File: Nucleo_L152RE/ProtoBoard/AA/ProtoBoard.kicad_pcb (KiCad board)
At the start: 2 copper layers, 7 parts, among them P1 SWD Header, P2 Power, U1 Nucleo-L152RE-CN7, U2 Nucleo-L152RE-CN10, U3 RFM69HW

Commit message: Have all footprints selected for components, now starting to organize parts on board.
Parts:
- added C10: 0.1u, Capacitors_SMD:C_0603, F.Cu at (-41.1, 7.87)
- added C11: 0.1u, Capacitors_SMD:C_0603, F.Cu at (-53.1, 9.65)
- added C12: 0.1u, Capacitors_SMD:C_0603, F.Cu at (-54.4, 16.3)
- added C3: 10uF, Capacitors_SMD:C_0603_HandSoldering, F.Cu at (-37.1, 16.3)
- added C4: 10uF, Capacitors_SMD:C_0603_HandSoldering, F.Cu at (-36.6, 14.0)
- added C5: 22uF, Capacitors_SMD:C_0603_HandSoldering, F.Cu at (-38.1, 6.35)
- added C6: 22uF, Capacitors_SMD:C_0603_HandSoldering, F.Cu at (-41.4, 4.06)
- added C7: 220uF, nucleo:Cap_alum_electro_3.3x3.3, F.Cu at (-42.7, 13.0)
- added C8: 0.1u, Capacitors_SMD:C_0603, F.Cu at (-36.3, 10.7)
- added C9: 0.1p, Capacitors_SMD:C_0603, F.Cu at (-47.2, 8.38)
- added D1: Red, nucleo:LED_0603, F.Cu at (-39.6, 19.8)
- added D2: Green, nucleo:LED_0603, F.Cu at (-42.7, 13.0)
- added J1: EXT1, nucleo:RJ45_SMD, F.Cu at (47.5, 2.54)
- added J2: USB, Connect:USB_B, F.Cu at (22.6, -4.32)
- added J3: EXT2, nucleo:RJ45_SMD, F.Cu at (46.0, -24.1)
- added JP1: Jumper_NC_Small, nucleo:SB_NC, F.Cu at (-48.0, 12.4)
- added JP10, JP11, JP13, JP15, JP16, JP17, JP18, JP19, JP20, JP21, JP22, JP23, JP24, JP25, JP26, JP27, JP28, JP29, JP30, JP31, JP38, JP39, JP4, JP40, JP41, JP42, JP5, JP6, JP7, JP8, JP9: Jumper_NC_Small, nucleo:SB_NC, F.Cu at (-42.7, 13.0)
- added JP12, JP14, JP32, JP33, JP34, JP35, JP36, JP37: Jumper_NO_Small, nucleo:SB_NO, F.Cu at (-42.7, 13.0)
- added JP2: Jumper_NC_Small, nucleo:SB_NC, F.Cu at (-42.2, 18.3)
- added JP3: Jumper_NC_Small, nucleo:SB_NC, F.Cu at (-55.1, 13.2)
- added L1: 4.7uH, nucleo:Inductor_4.7u, F.Cu at (-31.8, 3.56)
- added L2: 10uH, nucleo:Inductor_10u, F.Cu at (-23.9, -3.56)
- added L3, L4: 600 Ohm, Resistors_SMD:R_0603_HandSoldering, F.Cu at (-42.7, 13.0)
- added P10: CONN_01X06, Pin_Headers:Pin_Header_Straight_1x06, F.Cu at (0.00, 21.3)
- added P11: I2C1_B, Pin_Headers:Pin_Header_Straight_1x04, F.Cu at (31.8, 16.3)
- added P12: I2C2_B, Pin_Headers:Pin_Header_Straight_1x04, F.Cu at (36.8, 14.7)
- added P13: SW_1_6, Pin_Headers:Pin_Header_Straight_2x06, F.Cu at (-17.8, 18.3)
- added P14: WS_1_2, Pin_Headers:Pin_Header_Straight_2x02, F.Cu at (-29.2, 15.2)
- added P15: WS_3_4, Pin_Headers:Pin_Header_Straight_2x02, F.Cu at (-29.0, 22.4)
- added P16: MS2, Pin_Headers:Pin_Header_Straight_1x03, F.Cu at (-19.6, 6.60)
- added P17: OW1_B, Pin_Headers:Pin_Header_Straight_1x03, F.Cu at (14.5, 2.03)
- added P18: OW2_B, Pin_Headers:Pin_Header_Straight_1x03, F.Cu at (12.4, -7.62)
- added P19: I2C1_C, Pin_Headers:Pin_Header_Straight_1x04, F.Cu at (41.7, 14.7)
- added P20: I2C2_C, Pin_Headers:Pin_Header_Straight_1x04, F.Cu at (15.0, 18.3)
- added P21: MS3, Pin_Headers:Pin_Header_Straight_1x03, F.Cu at (-11.7, 5.59)
- added P22: OW3_A, Pin_Headers:Pin_Header_Straight_1x03, F.Cu at (8.64, 1.78)
- added P23: OW4_A, Pin_Headers:Pin_Header_Straight_1x03, F.Cu at (17.3, -17.0)
- added P24: MS4, Pin_Headers:Pin_Header_Straight_1x03, F.Cu at (-6.86, 4.83)
- added P25: OW3_B, Pin_Headers:Pin_Header_Straight_1x03, F.Cu at (1.78, -16.0)
- added P26: OW4_B, Pin_Headers:Pin_Header_Straight_1x03, F.Cu at (-3.56, -15.7)
- added P27: RGB1, Pin_Headers:Pin_Header_Straight_1x04, F.Cu at (8.64, 15.7)
- added P28: Ant, Pin_Headers:Pin_Header_Straight_1x01, F.Cu at (18.5, -34.0)
- added P3: SWD Header, Pin_Headers:Pin_Header_Straight_1x06, F.Cu at (-6.86, 18.8)
- added P4: USART1, Pin_Headers:Pin_Header_Straight_1x04, F.Cu at (5.08, 24.6)
- added P5: MS1, Pin_Headers:Pin_Header_Straight_1x03, F.Cu at (-16.3, 6.10)
- added P6: I2C1_A, Pin_Headers:Pin_Header_Straight_1x04, F.Cu at (20.3, 17.8)
- added P7: I2C2_A, Pin_Headers:Pin_Header_Straight_1x04, F.Cu at (25.9, 17.3)
- added P8: OW1_A, Pin_Headers:Pin_Header_Straight_1x03, F.Cu at (6.86, -15.2)
- added P9: OW2_A, Pin_Headers:Pin_Header_Straight_1x03, F.Cu at (12.2, -15.7)
- added Q1: SI2323DS, SMD_Packages:SOT-323, F.Cu at (-42.7, 13.0)
- added R1: 4.7k, Resistors_SMD:R_0603_HandSoldering, F.Cu at (-46.7, 17.5)
- added R10, R9: 33, Resistors_SMD:R_0603_HandSoldering, F.Cu at (-42.7, 13.0)
- added R11, R12, R32, R33, R34, R35, R47, R7: 0, Resistors_SMD:R_0603_HandSoldering, F.Cu at (-42.7, 13.0)
- added R13, R15: 100k, Resistors_SMD:R_0603_HandSoldering, F.Cu at (-42.7, 13.0)
- added R14, R16, R26, R27, R28, R29, R30, R31, R36: 10k, Resistors_SMD:R_0603_HandSoldering, F.Cu at (-42.7, 13.0)
- added R17: 4.7K, Resistors_SMD:R_0603_HandSoldering, F.Cu at (-42.7, 13.0)
- added R18: 2.2K, Resistors_SMD:R_0603_HandSoldering, F.Cu at (-42.7, 13.0)
- added R19: 680, Resistors_SMD:R_0603_HandSoldering, F.Cu at (-42.7, 13.0)
- added R2: 4.7k, Resistors_SMD:R_0603_HandSoldering, F.Cu at (-52.1, 6.10)
- added R20: 390, Resistors_SMD:R_0603_HandSoldering, F.Cu at (-42.7, 13.0)
- added R21, R22, R24, R25, R3, R37, R38, R40, R41, R8: 4.7k, Resistors_SMD:R_0603_HandSoldering, F.Cu at (-42.7, 13.0)
- added R23, R39, R42, R43: 220, Resistors_SMD:R_0603_HandSoldering, F.Cu at (-42.7, 13.0)
- added R4: 10K, Resistors_SMD:R_0603_HandSoldering, F.Cu at (-42.7, 13.0)
- added R44: 1K, Resistors_SMD:R_0603_HandSoldering, F.Cu at (-42.7, 13.0)
- added R45: 1k, Resistors_SMD:R_0603_HandSoldering, F.Cu at (-42.7, 13.0)
- added R5: 4.7k 1%, Resistors_SMD:R_0603_HandSoldering, F.Cu at (-42.7, 13.0)
- added R6: 6.8k 1%, Resistors_SMD:R_0603_HandSoldering, F.Cu at (-42.7, 13.0)
- added SW1: MomentarySwitch, nucleo:Tact_switch, F.Cu at (-14.0, -11.2)
- added U4: LM3670, SMD_Packages:SOT-353, F.Cu at (-50.5, 13.2)
- added U5: MT3329_GPS, nucleo:MT3329, F.Cu at (-32.3, -22.1)
- added U6: S25FL127S, SMD_Packages:SOIC-8-N, F.Cu at (-46.7, 2.03)
- added U7: RFM69HW, nucleo:RFM69HW, F.Cu at (1.02, -28.7)
- C1: value C -> 0.1u; footprint Capacitors_SMD:C_0805_HandSoldering -> Capacitors_SMD:C_0603_HandSoldering
- C2: value C -> 100uF; footprint Capacitors_SMD:C_0805_HandSoldering -> nucleo:Capacitor_7.2x7.2
- P1: value SWD Header -> Power; footprint Pin_Headers:Pin_Header_Straight_1x06 -> Pin_Headers:Pin_Header_Straight_1x02
- P2: value Power -> USART2; footprint Pin_Headers:Pin_Header_Straight_1x02 -> Pin_Headers:Pin_Header_Straight_1x04
- U1: value Nucleo-L152RE-CN7 -> TPS61222-5V; footprint Pin_Headers:Pin_Header_Straight_2x19 -> nucleo:SO-70
- U2: value Nucleo-L152RE-CN10 -> Nucleo-L152RE-CN7
- U3: value RFM69HW -> Nucleo-L152RE-CN10; footprint nucleo:RFM69HW -> Pin_Headers:Pin_Header_Straight_2x19
- moved U3 144.7 mm to (-2.29, 138.4)
- moved U1 83.2 mm to (88.4, 197.1)
- moved P2 80.1 mm to (68.1, 183.1)
- moved C1 53.1 mm to (169.4, 174.0)
- moved C2 34.5 mm to (139.7, 169.4)
- moved U2 24.1 mm to (174.2, 97.0)
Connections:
- C1 pad 1: +3V3 -> Net-(C1-Pad1)
- C1 pad 2: GNDREF -> /VBAT_Trig
- C2 pad 1: +3V3 -> /VBAT
- C2 pad 2: GNDREF -> GND
- P1 pad 1: (no net) -> /VBAT
- P1 pad 2: /PA14 -> GND
- P2 pad 1: /E5V -> +3V3
- P2 pad 2: /GND -> Net-(JP1-Pad2)
- U1 pad 1: (no net) -> /VBAT
- U1 pad 2: (no net) -> +5V
- U1 pad 3: (no net) -> GND
- U1 pad 4: (no net) -> +5V
- U1 pad 5: +3V3 -> Net-(L1-Pad2)
- U1 pad 6: /E5V -> /VBAT
- U2 pad 1: (no net) -> /EXT_SPI_CLK
- U2 pad 11: (no net) -> /EXT2_ADC
- U2 pad 13: (no net) -> /TMS
- U2 pad 14: (no net) -> /NRST
- U2 pad 15: (no net) -> /TCK
- U2 pad 17: (no net) -> /EXT1_SPI_CS
- U2 pad 19: (no net) -> GND
- U2 pad 2: (no net) -> /EXT_SPI_MISO
- U2 pad 20: /GND -> GND
- U2 pad 21: (no net) -> /EXT2_SPI_CS
- U2 pad 22: (no net) -> GND
- U2 pad 23: (no net) -> /StatusButton1
- U2 pad 28: (no net) -> /3.3V_Enable
- U2 pad 3: (no net) -> /EXT_SPI_MOSI
- U2 pad 30: (no net) -> /MotionSense1
- U2 pad 31: /PB3 -> (no net)
- U2 pad 32: (no net) -> /EXT1_GPIO
- U2 pad 34: (no net) -> /MotionSense2
- U2 pad 35: (no net) -> /WS3
- U2 pad 36: (no net) -> /MotionSense3
- U2 pad 37: (no net) -> /WS4
- U2 pad 38: (no net) -> /MotionSense4
- U2 pad 4: (no net) -> /GPS_RX
- U2 pad 5: (no net) -> VDD
- U2 pad 6: (no net) -> +5V
- U2 pad 8: (no net) -> GND
- U2 pad 9: /GND -> /EXT1_ADC
- U3 pad 1: (no net) -> /RGB_Red
- U3 pad 10: (no net) -> /GPS_TX
- U3 pad 11: (no net) -> /EXT2_GPIO
- U3 pad 12: (no net) -> /USB_DP
- U3 pad 13: (no net) -> /RGB_Green
- U3 pad 14: (no net) -> /USB_DM
- U3 pad 15: (no net) -> /RGB_Blue
- U3 pad 16: (no net) -> /SPI2_NSS
- U3 pad 2: (no net) -> /OneWireBus2
- U3 pad 3: (no net) -> /I2C_SCL1
- U3 pad 4: (no net) -> /OneWireBus3
- U3 pad 5: (no net) -> /I2C_SDA1
- U3 pad 6: (no net) -> /SWBus
- U3 pad 8: +3V3 -> /U5V
- U3 pad 9: (no net) -> GND

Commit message: Removed many jumper bridges, starting to get a feel for how many components there will be and where they will be.
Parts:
- removed J3: EXT2, nucleo:RJ45_SMD
- removed JP10, JP11, JP13, JP15, JP24, JP25, JP26, JP27, JP28, JP29, JP40: Jumper_NC_Small, nucleo:SB_NC
- removed JP12, JP14: Jumper_NO_Small, nucleo:SB_NO
- removed R29, R30, R31: 10k, Resistors_SMD:R_0603_HandSoldering
- removed R32, R33, R34, R47: 0, Resistors_SMD:R_0603_HandSoldering
- removed R45: 1k, Resistors_SMD:R_0603_HandSoldering
- added CON1: USB-MICRO-B, nucleo:USB_micro_AB, F.Cu at (169.1, 127.3)
- added D3: Green, nucleo:LED_0603, F.Cu at (69.5, 74.2)
- added D4: Blue, nucleo:LED_0603, F.Cu at (103.1, 33.6)
- added JP43: Jumper_NC_Small, nucleo:SB_NC, F.Cu at (-3.83, 84.8)
- added JP44: Jumper_NO_Small, nucleo:SB_NO, F.Cu at (8.65, 56.8)
- added JP53: Jumper_NC_Small, nucleo:SB_NC, F.Cu at (191.7, 47.1)
- added JP54: Jumper_NC_Small, nucleo:SB_NC, F.Cu at (189.9, 46.7)
- added JP55: Jumper_NC_Small, nucleo:SB_NC, F.Cu at (188.0, 46.7)
- added JP56: Jumper_NC_Small, nucleo:SB_NC, F.Cu at (185.8, 46.7)
- added JP57: Jumper_NC_Small, nucleo:SB_NC, F.Cu at (77.1, 13.4)
- added JP58: Jumper_NO_Small, nucleo:SB_NO, F.Cu at (3.63, 19.9)
- added JP59: Jumper_NC_Small, nucleo:SB_NC, F.Cu at (70.3, 30.3)
- added JP60: Jumper_NO_Small, nucleo:SB_NO, F.Cu at (29.1, 35.9)
- added P29: Ant, Pin_Headers:Pin_Header_Straight_1x01, F.Cu at (182.1, 42.3)
- C2: value 100uF -> 10uF; footprint nucleo:Capacitor_7.2x7.2 -> Capacitors_SMD:C_0603_HandSoldering
- D2: value Green -> Yellow
- J2: value USB -> EXT2; footprint Connect:USB_B -> nucleo:RJ45_SMD
- JP1: value Jumper_NC_Small -> BoostEn; footprint nucleo:SB_NC -> Pin_Headers:Pin_Header_Straight_1x02
- JP17, JP19, JP42, JP6, JP9: value Jumper_NC_Small -> Jumper_NO_Small; footprint nucleo:SB_NC -> nucleo:SB_NO
- JP32, JP34, JP36, JP37: value Jumper_NO_Small -> Jumper_NC_Small; footprint nucleo:SB_NO -> nucleo:SB_NC
- P10: value CONN_01X06 -> OW2_A; footprint Pin_Headers:Pin_Header_Straight_1x06 -> Pin_Headers:Pin_Header_Straight_1x03
- P11: value I2C1_B -> CONN_01X06; footprint Pin_Headers:Pin_Header_Straight_1x04 -> Pin_Headers:Pin_Header_Straight_1x06
- P12: value I2C2_B -> I2C1_B
- P13: value SW_1_6 -> I2C2_B; footprint Pin_Headers:Pin_Header_Straight_2x06 -> Pin_Headers:Pin_Header_Straight_1x04
- P14: value WS_1_2 -> SW_1_6; footprint Pin_Headers:Pin_Header_Straight_2x02 -> Pin_Headers:Pin_Header_Straight_2x06
- P15: value WS_3_4 -> WS_1_2
- P16: value MS2 -> WS_3_4; footprint Pin_Headers:Pin_Header_Straight_1x03 -> Pin_Headers:Pin_Header_Straight_2x02
- P17: value OW1_B -> MS2
- P18: value OW2_B -> OW1_B
- P19: value I2C1_C -> OW2_B; footprint Pin_Headers:Pin_Header_Straight_1x04 -> Pin_Headers:Pin_Header_Straight_1x03
- P2: value USART2 -> VinPower; footprint Pin_Headers:Pin_Header_Straight_1x04 -> Pin_Headers:Pin_Header_Straight_1x02
- P20: value I2C2_C -> I2C1_C
- P21: value MS3 -> I2C2_C; footprint Pin_Headers:Pin_Header_Straight_1x03 -> Pin_Headers:Pin_Header_Straight_1x04
- P22: value OW3_A -> MS3
- P23: value OW4_A -> OW3_A
- P24: value MS4 -> OW4_A
- P25: value OW3_B -> MS4
- P26: value OW4_B -> OW3_B
- P27: value RGB1 -> OW4_B; footprint Pin_Headers:Pin_Header_Straight_1x04 -> Pin_Headers:Pin_Header_Straight_1x03
- P28: value Ant -> RGB1; footprint Pin_Headers:Pin_Header_Straight_1x01 -> Pin_Headers:Pin_Header_Straight_1x04
- P3: value SWD Header -> USART2; footprint Pin_Headers:Pin_Header_Straight_1x06 -> Pin_Headers:Pin_Header_Straight_1x04
- P4: value USART1 -> SWD Header; footprint Pin_Headers:Pin_Header_Straight_1x04 -> Pin_Headers:Pin_Header_Straight_1x06
- P5: value MS1 -> USART1; footprint Pin_Headers:Pin_Header_Straight_1x03 -> Pin_Headers:Pin_Header_Straight_1x04
- P6: value I2C1_A -> MS1; footprint Pin_Headers:Pin_Header_Straight_1x04 -> Pin_Headers:Pin_Header_Straight_1x03
- P7: value I2C2_A -> I2C1_A
- P8: value OW1_A -> I2C2_A; footprint Pin_Headers:Pin_Header_Straight_1x03 -> Pin_Headers:Pin_Header_Straight_1x04
- P9: value OW2_A -> OW1_A
- R1: value 4.7k -> 10K
- R10, R9: value 33 -> 1k
- R12: value 0 -> 33
- R13: value 100k -> 0
- R14, R16: value 10k -> 100k
- R15: value 100k -> 10k
- R17: value 4.7K -> 2.2k
- R18: value 2.2K -> 2.2k
- R19: value 680 -> 2.2k
- R2: value 4.7k -> 4.7k 1%
- R20: value 390 -> 2.2k
- R21: value 4.7k -> 10k
- R22: value 4.7k -> 4.7K
- R23: value 220 -> 2.2K
- R24: value 4.7k -> 680
- R25: value 4.7k -> 390
- R26, R27: value 10k -> 4.7k
- R28: value 10k -> 220
- R3: value 4.7k -> 6.8k 1%
- R36: value 10k -> 0
- R37, R38: value 4.7k -> 0
- R39: value 220 -> 10k
- R4: value 10K -> 0
- R44: value 1K -> 220
- R5: value 4.7k 1% -> 33
- R6: value 6.8k 1% -> 0
- R7: value 0 -> 1K
- R8: value 4.7k -> 1k
- moved U6 255.4 mm to (180.4, 118.8)
- moved JP31 250.8 mm to (181.7, 124.8), turned to 270 degrees
- moved R16 249.7 mm to (179.4, 127.1), turned to 180 degrees
- moved JP21 249.1 mm to (180.0, 124.7), turned to 90 degrees
- moved JP20 247.6 mm to (178.3, 124.6), turned to 90 degrees
- moved JP23 246.4 mm to (182.7, 112.7), turned to 270 degrees
- moved JP22 244.9 mm to (181.0, 112.6), turned to 270 degrees
- moved JP30 243.6 mm to (179.6, 112.6), turned to 90 degrees
- moved R14 241.9 mm to (177.8, 112.5), turned to 270 degrees
- moved L3 235.0 mm to (166.0, 121.0)
- moved SW1 215.9 mm to (152.9, 125.8), turned to 180 degrees
- moved U5 214.7 mm to (167.2, 57.5), turned to 90 degrees
- moved U7 205.9 mm to (186.8, 60.1), turned to 90 degrees
- moved U4 199.5 mm to (140.2, 71.8), turned to 90 degrees
- moved C6 198.1 mm to (144.4, 72.6)
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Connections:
- C3 pad 1: +5V -> Net-(C3-Pad1)
- C4 pad 1: +5V -> /E5V
- J1 pad 3: Net-(J1-Pad3) -> /EXT1_SPI_CS
- J1 pad 4: Net-(J1-Pad4) -> /EXT_SPI_CLK
- J1 pad 5: Net-(J1-Pad5) -> /EXT_SPI_MOSI
- J1 pad 6: Net-(J1-Pad6) -> /EXT_SPI_MISO
- J1 pad 7: Net-(J1-Pad7) -> /EXT1_ADC
- J1 pad 8: Net-(J1-Pad8) -> /EXT1_GPIO
- J2 pad 2: Net-(J2-Pad2) -> GND
- J2 pad 3: Net-(J2-Pad3) -> /EXT2_SPI_CS
- J2 pad 4: GND -> /EXT_SPI_CLK
- J2 pad 5: Net-(J2-Pad5) -> /EXT_SPI_MOSI
- J2 pad 6: Net-(J2-Pad6) -> /EXT_SPI_MISO
- JP1 pad 1: /USART2_TX -> /E5V
- JP1 pad 2: Net-(JP1-Pad2) -> Net-(C3-Pad1)
- JP16 pad 1: /SPI2_MISO -> /GPS_RX
- JP17 pad 1: /SPI2_SCK -> /USART1_RX
- JP17 pad 2: Net-(JP17-Pad2) -> Net-(JP16-Pad2)
- JP18 pad 1: /SPI2_MOSI -> /GPS_TX
- JP19 pad 1: /EXT2_SPI_CS -> /USART1_TX
- JP19 pad 2: Net-(J3-Pad3) -> Net-(JP18-Pad2)
- JP2 pad 1: /USART2_RX -> /USART2_TX
- JP20 pad 1: /EXT_SPI_CLK -> /FLASH_nCS
- JP20 pad 2: Net-(J3-Pad4) -> Net-(JP20-Pad2)
- JP21 pad 1: /EXT_SPI_MOSI -> /SPI2_MISO
- JP21 pad 2: Net-(J3-Pad5) -> Net-(JP21-Pad2)
- JP22 pad 1: /EXT_SPI_MISO -> /SPI2_SCK
- JP22 pad 2: Net-(J3-Pad6) -> Net-(JP22-Pad2)
- JP23 pad 1: /EXT2_ADC -> /SPI2_MOSI
- JP23 pad 2: Net-(J3-Pad7) -> Net-(JP23-Pad2)
- JP3 pad 1: /USART1_TX -> /USART2_RX
- JP30 pad 1: /OneWireBus4 -> Net-(JP30-Pad1)
- JP30 pad 2: /OW4 -> Net-(JP30-Pad2)
- JP32 pad 1: Net-(JP32-Pad1) -> +3V3
- JP33 pad 1: Net-(JP33-Pad1) -> /E5V
- JP33 pad 2: Net-(JP33-Pad2) -> Net-(JP32-Pad2)
- JP34 pad 1: Net-(JP34-Pad1) -> +3V3
- JP35 pad 1: Net-(JP35-Pad1) -> /E5V
- JP35 pad 2: Net-(JP35-Pad2) -> Net-(JP34-Pad2)
- JP36 pad 1: Net-(JP36-Pad1) -> /OneWireBus1
- JP36 pad 2: Net-(JP36-Pad2) -> /OW1
- JP37 pad 1: Net-(JP37-Pad1) -> /OneWireBus2
- JP37 pad 2: Net-(JP37-Pad2) -> /OW2
- JP38 pad 1: +3V3 -> /OneWireBus3
- JP38 pad 2: Net-(JP38-Pad2) -> /OW3
- JP39 pad 1: Net-(JP39-Pad1) -> /OneWireBus4
- JP39 pad 2: /SPI2_NSS -> /OW4
- JP4 pad 1: /USART1_RX -> /USART1_TX
- JP41 pad 2: /SPI2_MISO -> +3V3
- JP42 pad 1: Net-(JP42-Pad1) -> Net-(JP41-Pad1)
- JP42 pad 2: /SPI2_SCK -> /E5V
- JP5 pad 1: /EXT1_SPI_CS -> /USART1_RX
- JP5 pad 2: Net-(J1-Pad3) -> Net-(JP5-Pad2)
- JP6 pad 1: /EXT_SPI_CLK -> /E5V
- JP6 pad 2: Net-(J1-Pad4) -> Net-(JP6-Pad2)
- JP7 pad 1: /EXT_SPI_MOSI -> /U5V
- JP7 pad 2: Net-(J1-Pad5) -> Net-(JP6-Pad2)
- JP8 pad 1: /EXT_SPI_MISO -> /StatusLed2
- JP8 pad 2: Net-(J1-Pad6) -> Net-(CON1-Pad4)
- JP9 pad 1: /EXT1_ADC -> GND
- JP9 pad 2: Net-(J1-Pad7) -> Net-(CON1-Pad4)
- L3 pad 1: Net-(J2-Pad5) -> GNDPWR
- L4 pad 1: Net-(J2-Pad6) -> GNDPWR
- P10 pad 1: Net-(JP32-Pad1) -> Net-(JP43-Pad1)
- P10 pad 2: Net-(JP33-Pad1) -> /OW2
- P10 pad 3: Net-(JP34-Pad1) -> GND
- P11 pad 1: +3V3 -> Net-(P11-Pad1)
- P11 pad 2: /I2C_SDA1 -> Net-(P11-Pad2)
- P11 pad 3: /I2C_SCL1 -> Net-(P11-Pad3)
- P11 pad 4: GND -> Net-(P11-Pad4)
- P12 pad 1: +3V3 -> Net-(JP32-Pad2)
- P12 pad 2: /I2C_SDA2 -> /I2C_SDA1
- P12 pad 3: /I2C_SCL2 -> /I2C_SCL1
- P13 pad 1: Net-(P13-Pad1) -> Net-(JP34-Pad2)
- P13 pad 2: Net-(P13-Pad2) -> /I2C_SDA2
- P13 pad 3: Net-(P13-Pad3) -> /I2C_SCL2
- P13 pad 4: Net-(P13-Pad4) -> GND
- P14 pad 1: /WS1 -> Net-(P14-Pad1)
- P14 pad 2: Net-(P14-Pad2) -> +3V3
- P14 pad 3: /WS2 -> Net-(P14-Pad3)
- P14 pad 4: Net-(P14-Pad4) -> +3V3
- P15 pad 1: /WS3 -> /WS1
- P15 pad 3: /WS4 -> /WS2
- P16 pad 1: +3V3 -> /WS3
- P16 pad 2: /MotionSense2 -> Net-(P16-Pad2)
- P16 pad 3: GND -> /WS4
- P17 pad 2: /OW1 -> /MotionSense2
- P18 pad 1: +3V3 -> Net-(JP41-Pad1)
- P18 pad 2: /OW2 -> /OW1
- P19 pad 1: +3V3 -> Net-(JP43-Pad1)
- P19 pad 2: /I2C_SDA1 -> /OW2
- P19 pad 3: /I2C_SCL1 -> GND
- P2 pad 1: +3V3 -> /VIN
- P2 pad 2: Net-(JP1-Pad2) -> GND
- P20 pad 1: +3V3 -> Net-(JP32-Pad2)
- P20 pad 2: /I2C_SDA2 -> /I2C_SDA1
- P20 pad 3: /I2C_SCL2 -> /I2C_SCL1
- P21 pad 1: +3V3 -> Net-(JP34-Pad2)
- P21 pad 2: /MotionSense3 -> /I2C_SDA2
- P21 pad 3: GND -> /I2C_SCL2
- P22 pad 2: /OW3 -> /MotionSense3
- P23 pad 1: +3V3 -> Net-(JP57-Pad1)
- P23 pad 2: /OW4 -> /OW3
- P24 pad 1: +3V3 -> Net-(JP59-Pad1)
- P24 pad 2: /MotionSense4 -> /OW4
- P25 pad 2: /OW3 -> /MotionSense4
- P26 pad 1: +3V3 -> Net-(JP57-Pad1)
- P26 pad 2: /OW4 -> /OW3
- P27 pad 1: +3V3 -> Net-(JP59-Pad1)
- P27 pad 2: Net-(P27-Pad2) -> /OW4
- P27 pad 3: Net-(P27-Pad3) -> GND
- P28 pad 1: Net-(P28-Pad1) -> +3V3
- P3 pad 1: (no net) -> +3V3
- P3 pad 2: /TCK -> Net-(JP2-Pad2)
- P3 pad 3: GND -> Net-(JP3-Pad2)
- P3 pad 4: /TMS -> GND
- P4 pad 1: +3V3 -> (no net)
- P4 pad 2: Net-(JP3-Pad2) -> /TCK
- P4 pad 3: Net-(JP4-Pad2) -> GND
- P4 pad 4: GND -> /TMS
- P5 pad 2: /MotionSense1 -> Net-(JP4-Pad2)
- P5 pad 3: GND -> Net-(JP5-Pad2)
- P6 pad 2: /I2C_SDA1 -> /MotionSense1
- P6 pad 3: /I2C_SCL1 -> GND
- P7 pad 1: +3V3 -> Net-(JP32-Pad2)
- P7 pad 2: /I2C_SDA2 -> /I2C_SDA1
- P7 pad 3: /I2C_SCL2 -> /I2C_SCL1
- P8 pad 1: +3V3 -> Net-(JP34-Pad2)
- P8 pad 2: /OW1 -> /I2C_SDA2
- P8 pad 3: GND -> /I2C_SCL2
- P9 pad 1: +3V3 -> Net-(JP41-Pad1)
- P9 pad 2: /OW2 -> /OW1
- R1 pad 1: +3V3 -> /VBAT
- R1 pad 2: /I2C_SDA1 -> Net-(C1-Pad1)
- R10 pad 1: /USB_DM -> /StatusLed4
- R10 pad 2: Net-(J2-Pad2) -> Net-(D4-Pad1)
- R11 pad 1: +3V3 -> Net-(CON1-Pad1)
- R11 pad 2: Net-(J1-Pad1) -> Net-(JP6-Pad2)
- R12 pad 1: +3V3 -> /USB_DM
- R13 pad 1: Net-(JP25-Pad2) -> +3V3
- R13 pad 2: +3V3 -> Net-(J2-Pad1)
- R14 pad 1: /SWBus -> Net-(JP30-Pad2)
- R14 pad 2: GND -> +3V3
- R15 pad 1: Net-(JP26-Pad2) -> /SWBus
- R15 pad 2: +3V3 -> GND
- R16 pad 1: Net-(P13-Pad1) -> Net-(JP31-Pad2)
- R16 pad 2: /SWBus -> +3V3
- R17 pad 1: Net-(P13-Pad3) -> Net-(JP32-Pad2)
- R17 pad 2: /SWBus -> /I2C_SCL1
- R18 pad 1: Net-(P13-Pad5) -> Net-(JP34-Pad2)
- R18 pad 2: /SWBus -> /I2C_SCL2
- R19 pad 1: Net-(P13-Pad7) -> Net-(JP32-Pad2)
- R19 pad 2: /SWBus -> /I2C_SDA1
- R2 pad 1: +3V3 -> Net-(Q1-Pad3)
- R2 pad 2: /I2C_SCL2 -> /VBAT_Meas
- R20 pad 1: Net-(P13-Pad9) -> Net-(JP34-Pad2)
- R20 pad 2: /SWBus -> /I2C_SDA2
- R21 pad 1: /OW1 -> Net-(P14-Pad1)
- R21 pad 2: +3V3 -> /SWBus
- R22 pad 1: /OW2 -> Net-(P14-Pad3)
- R22 pad 2: +3V3 -> /SWBus
- R23 pad 1: Net-(P13-Pad11) -> Net-(P14-Pad5)
- R24 pad 1: /OW1 -> Net-(P14-Pad7)
- R24 pad 2: +3V3 -> /SWBus
- R25 pad 1: /OW2 -> Net-(P14-Pad9)
- R25 pad 2: +3V3 -> /SWBus
- R26 pad 1: Net-(P13-Pad2) -> /OW1
- R26 pad 2: +3V3 -> Net-(JP41-Pad1)
- R27 pad 1: Net-(P13-Pad4) -> /OW2
- R27 pad 2: +3V3 -> Net-(JP43-Pad1)
- R28 pad 1: Net-(P13-Pad6) -> Net-(P14-Pad11)
- R28 pad 2: +3V3 -> /SWBus
- R3 pad 1: +3V3 -> /VBAT_Meas
- R3 pad 2: /I2C_SCL1 -> GND
- R35 pad 1: Net-(P15-Pad4) -> Net-(P15-Pad2)
- R36 pad 1: GND -> Net-(P15-Pad4)
- R36 pad 2: Net-(JP31-Pad1) -> +3V3
- R37 pad 1: /OW3 -> Net-(P16-Pad2)
- R38 pad 1: /OW4 -> Net-(P16-Pad4)
- R39 pad 1: Net-(P27-Pad2) -> GND
- R39 pad 2: /RGB_Red -> Net-(R39-Pad2)
- R4 pad 1: /VBAT -> +3V3
- R4 pad 2: Net-(C1-Pad1) -> VDD
- R40 pad 2: +3V3 -> Net-(JP57-Pad1)
- R41 pad 2: +3V3 -> Net-(JP59-Pad1)
- R42 pad 1: Net-(P27-Pad3) -> Net-(P28-Pad2)
- R42 pad 2: /RGB_Blue -> /RGB_Red
- R43 pad 1: Net-(P27-Pad4) -> Net-(P28-Pad3)
- R43 pad 2: /RGB_Green -> /RGB_Blue
- R44 pad 1: /StatusLed1 -> Net-(P28-Pad4)
- R44 pad 2: Net-(D1-Pad1) -> /RGB_Green
- R5 pad 1: Net-(Q1-Pad3) -> /USB_DP
- R5 pad 2: /VBAT_Meas -> Net-(CON1-Pad3)
- R6 pad 1: /VBAT_Meas -> +3V3
- R6 pad 2: GND -> Net-(J1-Pad1)
- R7 pad 1: +3V3 -> /StatusLed1
- R7 pad 2: VDD -> Net-(D1-Pad1)
- R8 pad 1: +3V3 -> /StatusLed2
- R8 pad 2: /I2C_SDA2 -> Net-(D2-Pad1)
- R9 pad 1: /USB_DP -> /StatusLed3
- R9 pad 2: Net-(J2-Pad3) -> Net-(D3-Pad1)
- U1 pad 2: +5V -> Net-(C3-Pad1)
- U1 pad 4: +5V -> Net-(C3-Pad1)
- U2 pad 24: (no net) -> /VIN
- U2 pad 26: (no net) -> +3V3
- U2 pad 6: +5V -> /E5V
- U3 pad 17: /GPS_Enable -> /StatusLed3
- U3 pad 23: /GPS_3D -> /StatusLed4
- U4 pad 1: +5V -> /E5V
- U5 pad 10: Net-(JP13-Pad2) -> Net-(JP18-Pad2)
- U5 pad 2: /GPS_Enable -> /StatusLed3
- U5 pad 5: /GPS_3D -> /StatusLed4
- U5 pad 9: Net-(JP11-Pad2) -> Net-(JP16-Pad2)
- U6 pad 1: Net-(JP15-Pad2) -> Net-(JP20-Pad2)
- U6 pad 2: Net-(JP16-Pad2) -> Net-(JP21-Pad2)
- U6 pad 3: Net-(JP26-Pad1) -> Net-(JP31-Pad1)
- U6 pad 5: Net-(JP18-Pad2) -> Net-(JP23-Pad2)
- U6 pad 6: Net-(JP17-Pad2) -> Net-(JP22-Pad2)
- U6 pad 7: Net-(JP25-Pad1) -> Net-(JP30-Pad1)
- U7 pad 1: Net-(JP31-Pad2) -> Net-(R39-Pad2)
- U7 pad 10: Net-(JP39-Pad1) -> Net-(JP53-Pad1)
- U7 pad 12: Net-(JP41-Pad1) -> Net-(JP55-Pad1)
- U7 pad 13: Net-(JP42-Pad1) -> Net-(JP56-Pad1)
- U7 pad 15: Net-(P28-Pad1) -> Net-(P29-Pad1)
- U7 pad 2: Net-(JP32-Pad2) -> Net-(P11-Pad1)
- U7 pad 3: Net-(JP33-Pad2) -> Net-(P11-Pad2)
- U7 pad 4: Net-(JP34-Pad2) -> Net-(P11-Pad3)
- U7 pad 5: Net-(JP35-Pad2) -> Net-(P11-Pad4)
- U7 pad 6: Net-(JP36-Pad2) -> Net-(P11-Pad5)
- U7 pad 7: Net-(JP37-Pad2) -> Net-(P11-Pad6)
- U7 pad 8: Net-(JP38-Pad2) -> +3V3
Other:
- board outline added: 70.5 x 55.4 mm

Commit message: About to remove a few extra connectors.
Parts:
- removed C2, C3, C4: 10uF, Capacitors_SMD:C_0603_HandSoldering
- removed C5, C6: 22uF, Capacitors_SMD:C_0603_HandSoldering
- removed C7: 220uF, nucleo:Cap_alum_electro_3.3x3.3
- removed JP1: BoostEn, Pin_Headers:Pin_Header_Straight_1x02
- removed L1: 4.7uH, nucleo:Inductor_4.7u
- removed L2: 10uH, nucleo:Inductor_10u
- removed R4: 0, Resistors_SMD:R_0603_HandSoldering
- removed U1: TPS61222-5V, nucleo:SO-70
- removed U4: LM3670, SMD_Packages:SOT-353
- added J3: EXTPower, nucleo:RJ45_SMD, F.Cu at (132.3, 15.1)
- C1, JP17, JP18, JP19, JP38, Q1, R2, R3, R40: moved to B.Cu
- moved P21 201.4 mm to (205.4, 86.0)
- moved P13 201.4 mm to (201.7, 85.8)
- moved P8 201.4 mm to (197.2, 86.0)
- moved P12 191.6 mm to (163.5, 61.1)
- moved P7 191.6 mm to (160.2, 60.8)
- moved P20 190.2 mm to (167.0, 60.8)
- moved JP16 174.7 mm to (157.0, 94.0), turned to 90 degrees
- moved P10 170.5 mm to (208.6, 125.1)
- moved P19 170.5 mm to (212.5, 125.1)
- moved P3 170.5 mm to (195.6, 136.2)
- moved P5 170.5 mm to (190.6, 136.6)
- moved P9 170.5 mm to (198.2, 125.5)
- moved P18 170.5 mm to (202.0, 125.5)
- moved JP6 159.5 mm to (161.8, 109.7)
- moved JP9 153.0 mm to (165.9, 111.8)
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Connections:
- net /VBAT_Trig renamed /VIN_Trig
- P1 pad 1: /VBAT -> /E5V
- P2 pad 1: /VIN -> +15V
- Q1 pad 2: /VBAT -> +15V
- R1 pad 1: /VBAT -> +15V
- R2 pad 2: /VBAT_Meas -> /VIN_Meas
- R3 pad 1: /VBAT_Meas -> /VIN_Meas
- U2 pad 24: /VIN -> +15V
- U2 pad 26: +3V3 -> (no net)
- U2 pad 28: /3.3V_Enable -> /VIN_Meas
- U2 pad 5: VDD -> +3V3
- U5 pad 5: /StatusLed4 -> (no net)

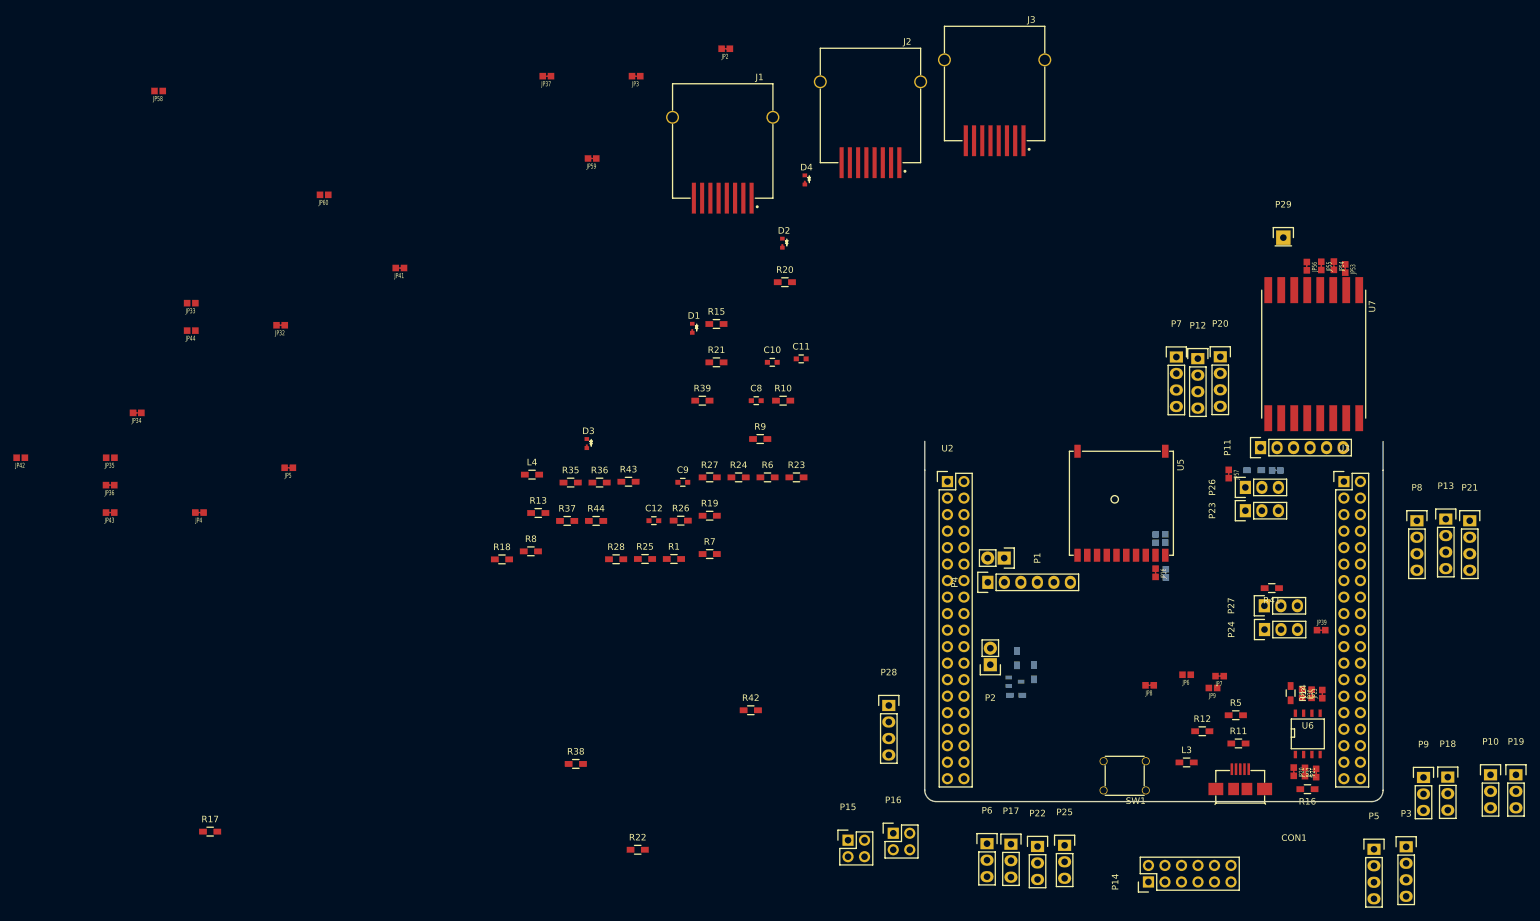
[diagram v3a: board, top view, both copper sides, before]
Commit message: all remaining components fit on one board.
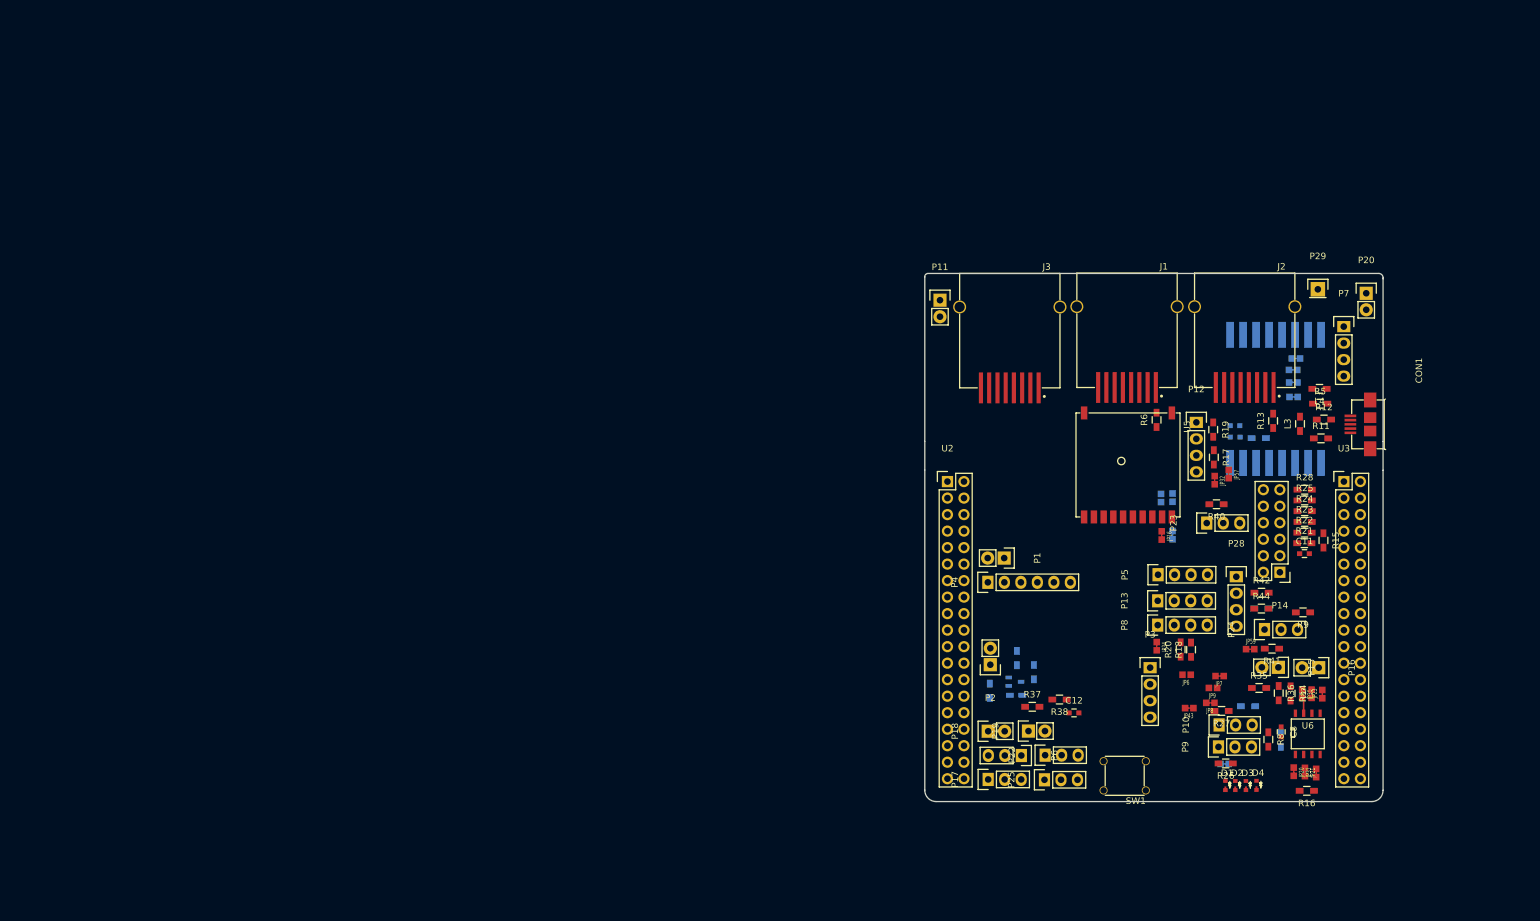
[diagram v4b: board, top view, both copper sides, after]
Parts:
- removed JP2, JP3, JP36, JP37, JP38, JP39, JP4, JP5: Jumper_NC_Small, nucleo:SB_NC
- removed JP33, JP35, JP42, JP44, JP58, JP60: Jumper_NO_Small, nucleo:SB_NO
- removed P21: I2C2_C, Pin_Headers:Pin_Header_Straight_1x04
- removed P26: OW3_B, Pin_Headers:Pin_Header_Straight_1x03
- removed P27: OW4_B, Pin_Headers:Pin_Header_Straight_1x03
- C10, C9, JP41, JP53, JP54, JP55, JP56, R1, R10, R39, R43, R7, U7: moved to B.Cu
- P11: value CONN_01X06 -> GND1; footprint Pin_Headers:Pin_Header_Straight_1x06 -> Pin_Headers:Pin_Header_Straight_1x02
- P15: value WS_1_2 -> WS1; footprint Pin_Headers:Pin_Header_Straight_2x02 -> Pin_Headers:Pin_Header_Straight_1x02
- P16: value WS_3_4 -> WS2; footprint Pin_Headers:Pin_Header_Straight_2x02 -> Pin_Headers:Pin_Header_Straight_1x02
- P18: value OW1_B -> WS3; footprint Pin_Headers:Pin_Header_Straight_1x03 -> Pin_Headers:Pin_Header_Straight_1x02
- P19: value OW2_B -> WS4; footprint Pin_Headers:Pin_Header_Straight_1x03 -> Pin_Headers:Pin_Header_Straight_1x02
- P20: value I2C1_C -> GND2; footprint Pin_Headers:Pin_Header_Straight_1x04 -> Pin_Headers:Pin_Header_Straight_1x02
- R40: moved to F.Cu
- moved JP43 168.7 mm to (162.2, 114.9)
- moved R17 164.8 mm to (166.0, 76.3), turned to 270 degrees
- moved JP34 160.9 mm to (157.2, 105.3), turned to 90 degrees
- moved JP41 148.1 mm to (167.6, 123.4)
- moved JP32 145.7 mm to (166.1, 79.8), turned to 90 degrees
- moved JP59 126.3 mm to (171.6, 105.8), turned to 180 degrees
- moved L4 121.9 mm to (182.2, 65.7), turned to 180 degrees
- moved R8 117.1 mm to (174.4, 119.7), turned to 270 degrees
- moved D4 116.2 mm to (172.5, 126.7)
- moved D3 114.2 mm to (170.9, 126.8)
- moved R13 114.0 mm to (175.1, 70.7), turned to 90 degrees
- moved R22 113.6 mm to (179.9, 87.9)
- moved R35 110.5 mm to (172.9, 111.8)
- moved R36 109.4 mm to (176.0, 112.5), turned to 270 degrees
- moved D2 108.7 mm to (169.3, 126.8)
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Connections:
- P10 pad 2: /OW2 -> /OneWireBus2
- P11 pad 1: Net-(P11-Pad1) -> GND
- P11 pad 2: Net-(P11-Pad2) -> GND
- P16 pad 1: /WS3 -> /WS2
- P18 pad 1: Net-(JP41-Pad1) -> /WS3
- P18 pad 2: /OW1 -> Net-(P18-Pad2)
- P19 pad 1: Net-(JP43-Pad1) -> /WS4
- P19 pad 2: /OW2 -> Net-(P19-Pad2)
- P20 pad 1: Net-(JP32-Pad2) -> GND
- P20 pad 2: /I2C_SDA1 -> GND
- P23 pad 2: /OW3 -> /OneWireBus3
- P24 pad 2: /OW4 -> /OneWireBus4
- P3 pad 2: Net-(JP2-Pad2) -> /USART2_TX
- P3 pad 3: Net-(JP3-Pad2) -> (no net)
- P5 pad 2: Net-(JP4-Pad2) -> /USART1_TX
- P5 pad 3: Net-(JP5-Pad2) -> /USART1_RX
- P9 pad 2: /OW1 -> /OneWireBus1
- R26 pad 1: /OW1 -> /OneWireBus1
- R27 pad 1: /OW2 -> /OneWireBus2
- R36 pad 1: Net-(P15-Pad4) -> Net-(P16-Pad2)
- R37 pad 1: Net-(P16-Pad2) -> Net-(P18-Pad2)
- R38 pad 1: Net-(P16-Pad4) -> Net-(P19-Pad2)
- R40 pad 1: /OW3 -> /OneWireBus3
- R41 pad 1: /OW4 -> /OneWireBus4
- U3 pad 37: /USART2_RX -> (no net)
- U7 pad 2: Net-(P11-Pad1) -> (no net)
- U7 pad 3: Net-(P11-Pad2) -> (no net)
- U7 pad 4: Net-(P11-Pad3) -> (no net)
- U7 pad 5: Net-(P11-Pad4) -> (no net)
- U7 pad 6: Net-(P11-Pad5) -> (no net)
- U7 pad 7: Net-(P11-Pad6) -> (no net)
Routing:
- net Net-(JP30-Pad1): track 0.00 -> 2.46 mm
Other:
- board size 70.5 x 55.4 mm -> 70.5 x 81.3 mm
- net class Default: trace_width 0.25 -> 0.254
